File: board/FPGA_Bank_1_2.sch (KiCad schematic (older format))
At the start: 3 parts, among them SW1 SW_PUSH, U10 XC6SLX150T

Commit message: Issue #1481 - DOC
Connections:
- net MDIO is gone; now on net MAC_SCL: U10.U10 (*IO_L46N_2)
- net MAC_SCL: no longer U10.V7 (*IO_L58P_2)
- net MAC_SDA: now also U10.T10 (*IO_L46P_2); no longer U10.W8 (*IO_L58N_2)
- net CLK_125NDO: no longer names the net of U10.Y13 (IO_L30P_GCLK1_D13_2)
- net INIT_N renamed ETH_RESET_B
- net RESET_B renamed ETH_MDIO
- net RXD0 renamed ETH_RXD0
- net RXD1 renamed ETH_RXD1
- net RXD2 renamed ETH_RXD2
- net RXD3 renamed ETH_RXD3
- net RX_DV renamed ETH_INT_B
- net TXD0 renamed ETH_TXD0
- net TXD1 renamed ETH_TXD1
- net TXD2 renamed ETH_TXD2
- net TXD3 renamed ETH_TXD3
- net TX_EN renamed ETH_RXCTL
- new net ETH_MDC: U10.V7 (*IO_L58P_2)
- new net ETH_TXCTL: U10.W8 (*IO_L58N_2)
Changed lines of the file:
@@
 LIBS:contrib
 LIBS:valves
+LIBS:hdmi2usb
 LIBS:HDMI2USB-cache
+LIBS:Atlys-VHDCI-cache
 EELAYER 27 0
 EELAYER END
 $Descr A2 23386 16535
 encoding utf-8
-Sheet 10 11
+Sheet 11 12
 Title "HDMI2USB"
-Date "14 jan 2015"
+Date "18 feb 2015"
 Rev "Rev2"
 Comp ""
@@
 	8250 14500 8250 14600
 $Comp
-L GND #PWR42
+L GND #PWR045
 U 1 1 53857D31
 P 8250 14600
-F 0 "#PWR42" H 8250 14600 30  0001 C CNN
+F 0 "#PWR045" H 8250 14600 30  0001 C CNN
 F 1 "GND" H 8250 14530 30  0001 C CNN
 F 2 "" H 8250 14600 60  0000 C CNN
@@
 Text HLabel 12450 4450 2    60   BiDi ~ 0
 CYPRESS-RESET
-Text HLabel 7400 7750 2    60   BiDi ~ 0
-TXD[0..3]
-Text HLabel 7250 9000 2    60   BiDi ~ 0
-RXD[0..3]
 Text HLabel 6100 5700 2    60   Output ~ 0
 GTP_CLK
-Text HLabel 6100 8100 2    60   Output ~ 0
-TX_EN
-Text HLabel 6150 7300 2    60   Output ~ 0
-MDC
-Text HLabel 6100 7400 2    60   BiDi ~ 0
-MDIO
 Text HLabel 6100 5800 2    60   Output ~ 0
 RX_CLK
-Text HLabel 6100 8200 2    60   Output ~ 0
-RX_DV
-Text HLabel 6100 8300 2    60   Output ~ 0
-INIT_N
-Text HLabel 6100 8400 2    60   Output ~ 0
-RESET_B
-Text HLabel 6100 8500 2    60   Output ~ 0
-MAC_SCL
-Text HLabel 6100 8600 2    60   BiDi ~ 0
-MAC_SDA
-Text HLabel 6100 5500 2    60   BiDi ~ 0
-CLK_125NDO
-Text Label 6350 7700 2    60   ~ 0
-TXD0
-Text Label 6350 7800 2    60   ~ 0
-TXD1
-Text Label 6350 7900 2    60   ~ 0
-TXD2
-Text Label 6350 8000 2    60   ~ 0
-TXD3
-Text Label 6350 9000 2    60   ~ 0
-RXD3
-Text Label 6350 8900 2    60   ~ 0
-RXD2
-Text Label 6350 8800 2    60   ~ 0
-RXD1
-Text Label 6350 8700 2    60   ~ 0
-RXD0
-Wire Wire Line
-	6100 7700 7150 7700
-Wire Wire Line
-	6100 7800 7150 7800
-Wire Wire Line
-	6100 7900 7150 7900
-Wire Wire Line
-	6100 8000 7150 8000
+Text Label 6550 7700 2    60   ~ 0
+ETH_TXD0
+Text Label 6550 7800 2    60   ~ 0
+ETH_TXD1
+Text Label 6550 7900 2    60   ~ 0
+ETH_TXD2
+Text Label 6550 8000 2    60   ~ 0
+ETH_TXD3
+Text Label 6550 9000 2    60   ~ 0
+ETH_RXD3
+Text Label 6550 8900 2    60   ~ 0
+ETH_RXD2
+Text Label 6550 8800 2    60   ~ 0
+ETH_RXD1
+Text Label 6550 8700 2    60   ~ 0
+ETH_RXD0
 Wire Wire Line
 	6100 8700 6850 8700
@@
 Wire Bus Line
 	6950 9000 7250 9000
+Text HLabel 6150 8100 2    47   Input ~ 0
+ETH_RXCTL
+Text HLabel 8800 8450 0    47   Input ~ 0
+ETH_RXCLK
+Text HLabel 7250 9000 2    60   Input ~ 0
+ETH_RXD[0..3]
+Text HLabel 6150 8500 2    47   Input ~ 0
+ETH_MDC
+Text HLabel 6150 8400 2    47   Input ~ 0
+ETH_MDIO
+Text HLabel 6150 8300 2    47   Input ~ 0
+ETH_RESET_B
+Text HLabel 6150 8200 2    47   Input ~ 0
+ETH_INT_B
+Text HLabel 8800 8550 0    47   Input ~ 0
+ETH_TXCLK
+Text HLabel 6150 8600 2    47   Input ~ 0
+ETH_TXCTL
+Text HLabel 7400 7750 2    60   Input ~ 0
+ETH_TXD[0..3]
+Text HLabel 8800 8350 0    47   Input ~ 0
+FPGA_CLK
+Text HLabel 6150 7400 2    47   Input ~ 0
+MAC_SCL
+Text HLabel 6150 7300 2    47   Input ~ 0
+MAC_SDA
+Wire Wire Line
+	6150 8100 6100 8100
+Wire Wire Line
+	6100 8200 6150 8200
+Wire Wire Line
+	6150 8300 6100 8300
+Wire Wire Line
+	6100 8400 6150 8400
+Wire Wire Line
+	6150 8500 6100 8500
+Wire Wire Line
+	6150 8600 6100 8600
+Wire Wire Line
+	6150 7300 6100 7300
+Wire Wire Line
+	6100 7400 6150 7400
+Text HLabel 8800 8650 0    47   Input ~ 0
+SYSCLK
+Wire Wire Line
+	6100 8000 7150 8000
+Wire Wire Line
+	6100 7900 7150 7900
+Wire Wire Line
+	6100 7800 7150 7800
+Wire Wire Line
+	6100 7700 7150 7700
 $EndSCHEMATC

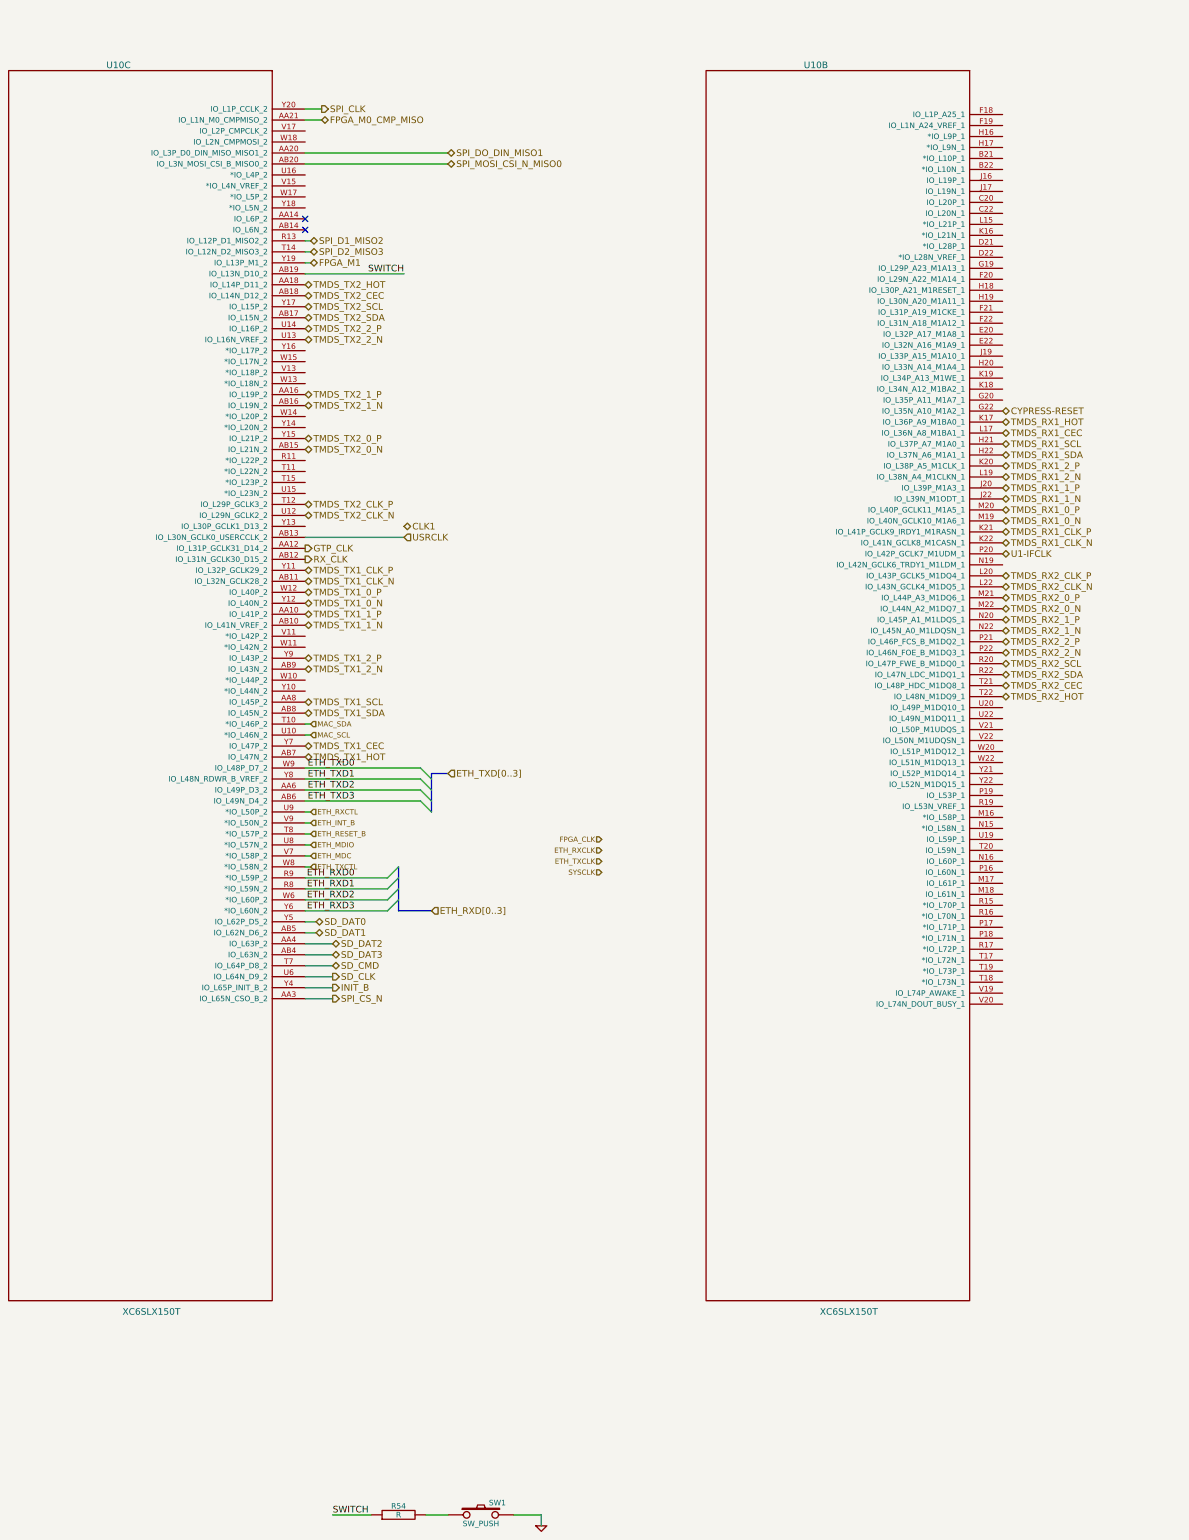
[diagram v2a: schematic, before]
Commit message: Issue #1481 - CYPRESS-FPGA CONNECTIONS ADDED
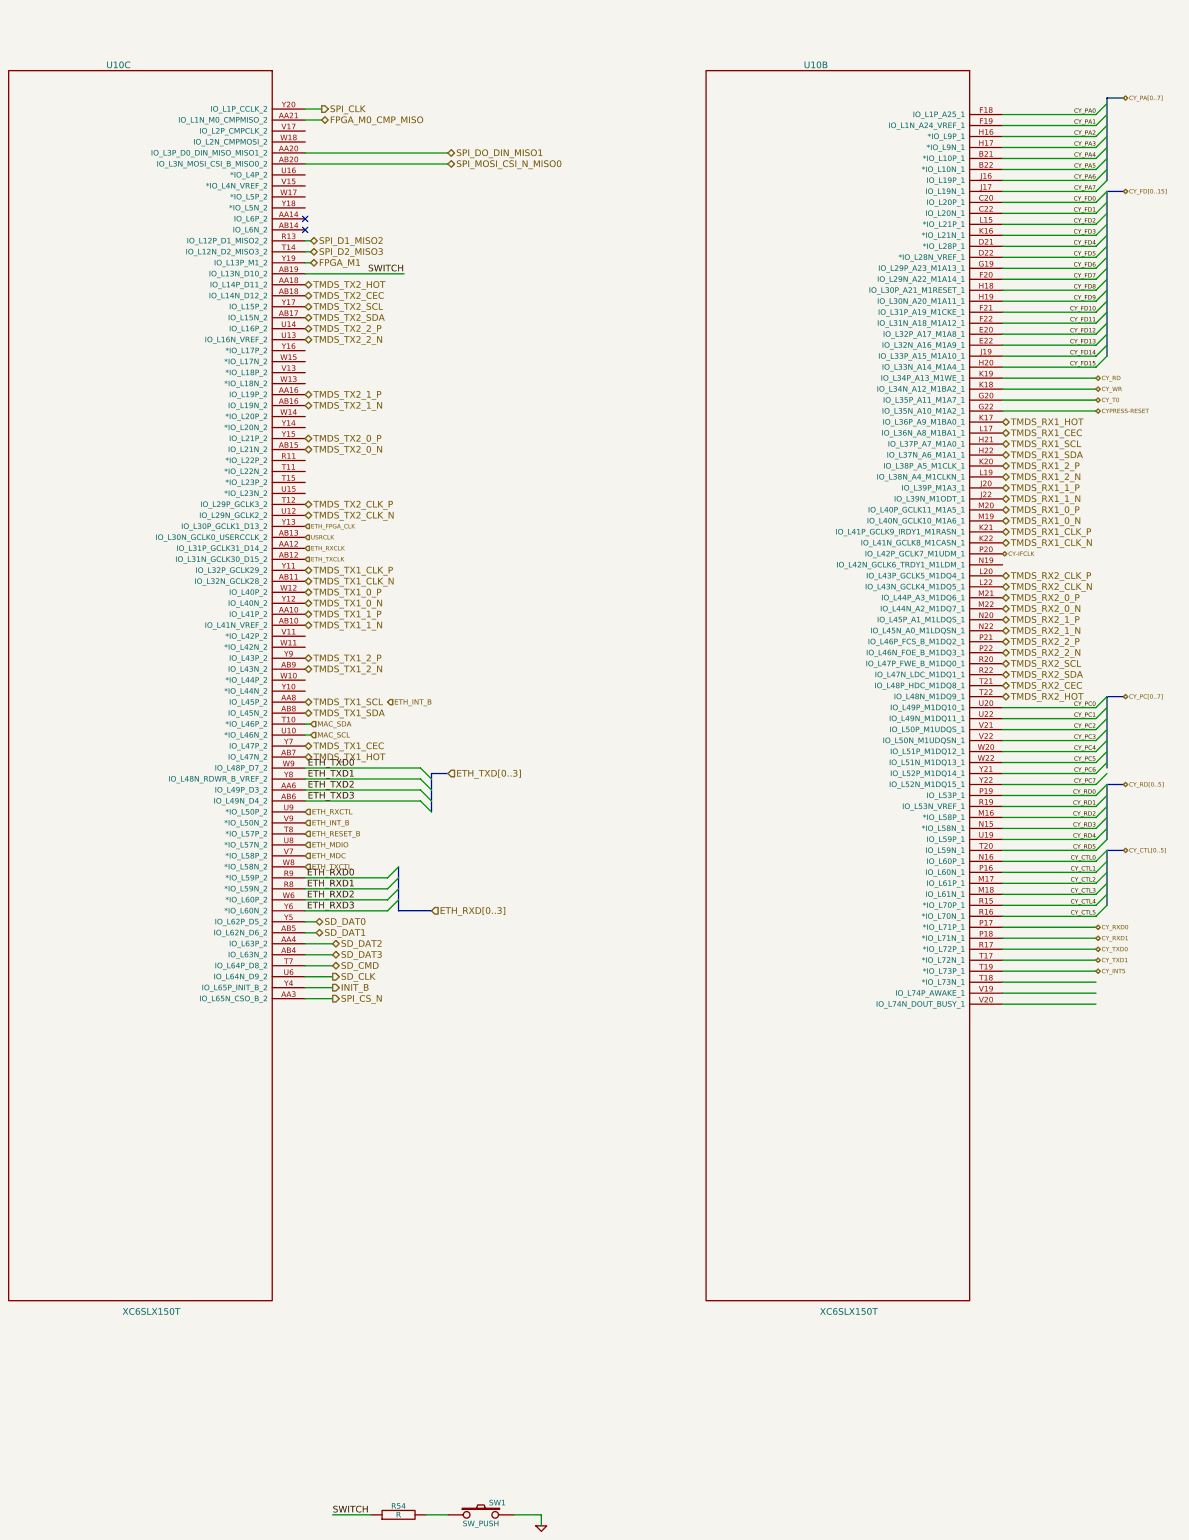
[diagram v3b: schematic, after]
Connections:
- net GTP_CLK is gone; now on net ETH_RXCLK: U10.AA12 (IO_L31P_GCLK31_D14_2)
- net RX_CLK is gone; now on net ETH_TXCLK: U10.AB12 (IO_L31N_GCLK30_D15_2)
- net ETH_FPGA_CLK: now reaches U10.Y13 (IO_L30P_GCLK1_D13_2)
- net CY_PA4: now reaches U10.B21 (*IO_L10P_1)
- net CY_PA5: now reaches U10.B22 (*IO_L10N_1)
- net CY_FD0: now reaches U10.C20 (IO_L20P_1)
- net CY_FD1: now reaches U10.C22 (IO_L20N_1)
- net CY_FD4: now reaches U10.D21 (*IO_L28P_1)
- net CY_FD5: now reaches U10.D22 (*IO_L28N_VREF_1)
- net CY_FD12: now reaches U10.E20 (IO_L32P_A17_M1A8_1)
- net CY_FD13: now reaches U10.E22 (IO_L32N_A16_M1A9_1)
- net CY_PA0: now reaches U10.F18 (IO_L1P_A25_1)
- net CY_PA1: now reaches U10.F19 (IO_L1N_A24_VREF_1)
- net CY_FD7: now reaches U10.F20 (IO_L29N_A22_M1A14_1)
- net CY_FD10: now reaches U10.F21 (IO_L31P_A19_M1CKE_1)
- net CY_FD11: now reaches U10.F22 (IO_L31N_A18_M1A12_1)
- net CY_FD6: now reaches U10.G19 (IO_L29P_A23_M1A13_1)
- net CY_T0: now reaches U10.G20 (IO_L35P_A11_M1A7_1)
- net CY_PA2: now reaches U10.H16 (*IO_L9P_1)
- net CY_PA3: now reaches U10.H17 (*IO_L9N_1)
- net CY_FD8: now reaches U10.H18 (IO_L30P_A21_M1RESET_1)
- net CY_FD9: now reaches U10.H19 (IO_L30N_A20_M1A11_1)
- net CY_FD15: now reaches U10.H20 (IO_L33N_A14_M1A4_1)
- net CY_PA6: now reaches U10.J16 (IO_L19P_1)
- net CY_PA7: now reaches U10.J17 (IO_L19N_1)
- net CY_FD14: now reaches U10.J19 (IO_L33P_A15_M1A10_1)
- net CY_FD3: now reaches U10.K16 (*IO_L21N_1)
- net CY_WR: now reaches U10.K18 (IO_L34N_A12_M1BA2_1)
- net CY_RD: now reaches U10.K19 (IO_L34P_A13_M1WE_1)
- net CY_FD2: now reaches U10.L15 (*IO_L21P_1)
- net CY_RD2: now reaches U10.M16 (*IO_L58P_1)
- net CY_CTL2: now reaches U10.M17 (IO_L61P_1)
- net CY_CTL3: now reaches U10.M18 (IO_L61N_1)
- net CY_RD3: now reaches U10.N15 (*IO_L58N_1)
- net CY_CTL0: now reaches U10.N16 (IO_L60P_1)
- net CY_CTL1: now reaches U10.P16 (IO_L60N_1)
- net CY_RXD0: now reaches U10.P17 (*IO_L71P_1)
- net CY_RXD1: now reaches U10.P18 (*IO_L71N_1)
- net CY_RD0: now reaches U10.P19 (IO_L53P_1)
- net CY_CTL4: now reaches U10.R15 (*IO_L70P_1)
- net CY_CTL5: now reaches U10.R16 (*IO_L70N_1)
- net CY_TXD0: now reaches U10.R17 (*IO_L72P_1)
- net CY_RD1: now reaches U10.R19 (IO_L53N_VREF_1)
- net CY_TXD1: now reaches U10.T17 (*IO_L72N_1)
- net CY_INT5: now reaches U10.T19 (*IO_L73P_1)
- net CY_RD5: now reaches U10.T20 (IO_L59N_1)
- net CY_RD4: now reaches U10.U19 (IO_L59P_1)
- net CY_PC0: now reaches U10.U20 (IO_L49P_M1DQ10_1)
- net CY_PC1: now reaches U10.U22 (IO_L49N_M1DQ11_1)
- net CY_PC2: now reaches U10.V21 (IO_L50P_M1UDQS_1)
- net CY_PC3: now reaches U10.V22 (IO_L50N_M1UDQSN_1)
- net CY_PC4: now reaches U10.W20 (IO_L51P_M1DQ12_1)
- net CY_PC5: now reaches U10.W22 (IO_L51N_M1DQ13_1)
- net CY_PC6: now reaches U10.Y21 (IO_L52P_M1DQ14_1)
- net CY_PC7: now reaches U10.Y22 (IO_L52N_M1DQ15_1)
- net U1-IFCLK renamed CY-IFCLK

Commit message: Issue #1412 - Placement
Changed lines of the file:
@@
 LIBS:valves
 LIBS:hdmi2usb
-LIBS:timvideos-pcie-8x
 LIBS:HDMI2USB-cache
 EELAYER 27 0
@@
 Sheet 12 12
 Title "HDMI2USB"
-Date "24 feb 2015"
+Date "27 feb 2015"
 Rev "Rev2"
 Comp ""
@@
 	13400 7850 13550 7850
 Wire Bus Line
-	13400 7700 13400 7050
+	13400 7050 13400 7750
 Wire Bus Line
 	13400 7050 13550 7050

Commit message: Issue #1608 - Placement
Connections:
- net CY_CTL2: now also U10.R15 (*IO_L70P_1); no longer U10.M17 (IO_L61P_1)
- net CY_CTL4: now also U10.M17 (IO_L61P_1); no longer U10.R15 (*IO_L70P_1)
- net SD_DAT2: now also U10.AB4 (IO_L63N_2); no longer U10.AA4 (IO_L63P_2)
- net SD_DAT3: now also U10.AA4 (IO_L63P_2); no longer U10.AB4 (IO_L63N_2)
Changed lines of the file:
@@
 Sheet 12 12
 Title "HDMI2USB"
-Date "27 feb 2015"
+Date "2 mar 2015"
 Rev "Rev2"
 Comp ""
@@
 Text HLabel 6200 9200 2    60   BiDi ~ 0
 SD_DAT1
+Text HLabel 6350 9400 2    60   BiDi ~ 0
+SD_DAT2
 Text HLabel 6350 9300 2    60   BiDi ~ 0
-SD_DAT2
-Text HLabel 6350 9400 2    60   BiDi ~ 0
 SD_DAT3
 Text HLabel 6350 9500 2    60   BiDi ~ 0
@@
 Text Label 13300 8650 2    39   ~ 0
 CY_CTL1
-Text Label 13300 8750 2    39   ~ 0
+Text Label 13300 8950 2    39   ~ 0
 CY_CTL2
 Text Label 13300 8850 2    39   ~ 0
 CY_CTL3
-Text Label 13300 8950 2    39   ~ 0
+Text Label 13300 8750 2    39   ~ 0
 CY_CTL4
 Text Label 13300 9050 2    39   ~ 0

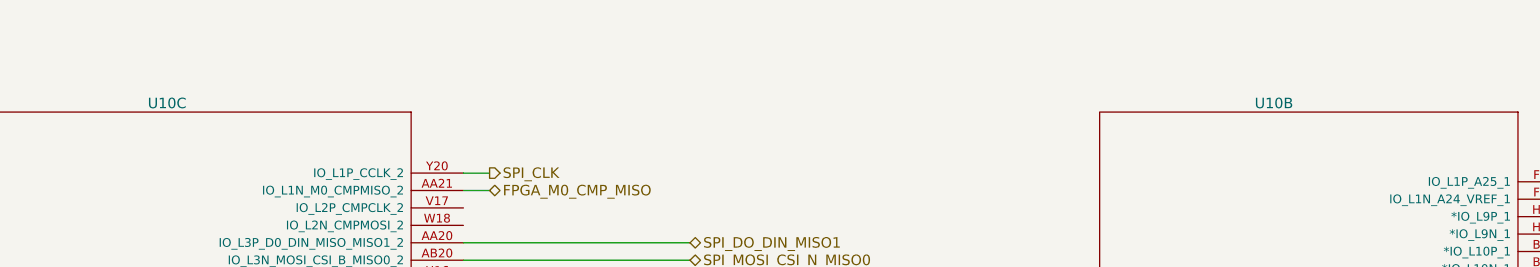
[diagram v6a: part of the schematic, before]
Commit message: Issue #1605 - Cypress routing
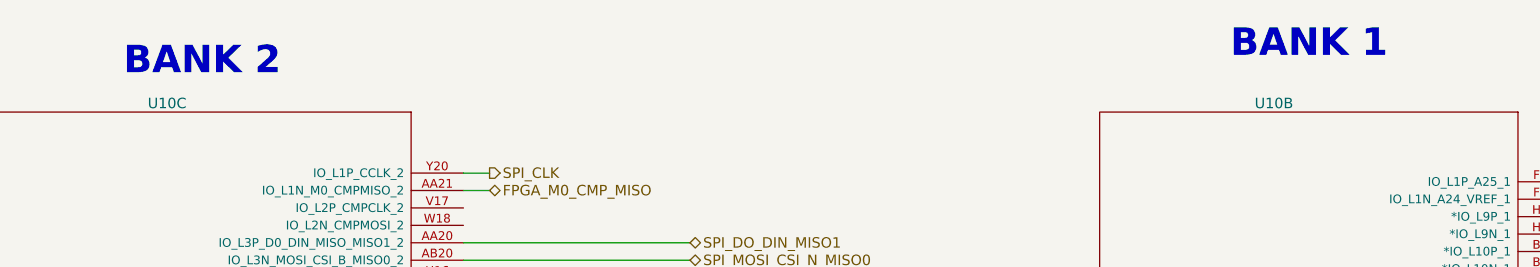
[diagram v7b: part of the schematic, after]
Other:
- note added: "BANK 1"
- note added: "BANK 2"
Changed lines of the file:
@@
 LIBS:valves
 LIBS:hdmi2usb
+LIBS:timvideos-pcie-8x
 LIBS:HDMI2USB-cache
 EELAYER 27 0
@@
 Sheet 12 12
 Title "HDMI2USB"
-Date "5 mar 2015"
+Date "11 mar 2015"
 Rev "Rev2"
 Comp ""
@@
 Text Label 13300 4050 2    39   ~ 0
 CY_FD15
+Text Notes 4150 1150 0    157  ~ 31
+BANK 2
+Text Notes 10500 1050 0    157  ~ 31
+BANK 1
 $EndSCHEMATC
